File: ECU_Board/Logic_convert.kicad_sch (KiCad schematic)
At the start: 25 parts, among them U10 LM324A, U11 LM324A, U12 CD4504B, U13 CD4504B, U14 CD4504B

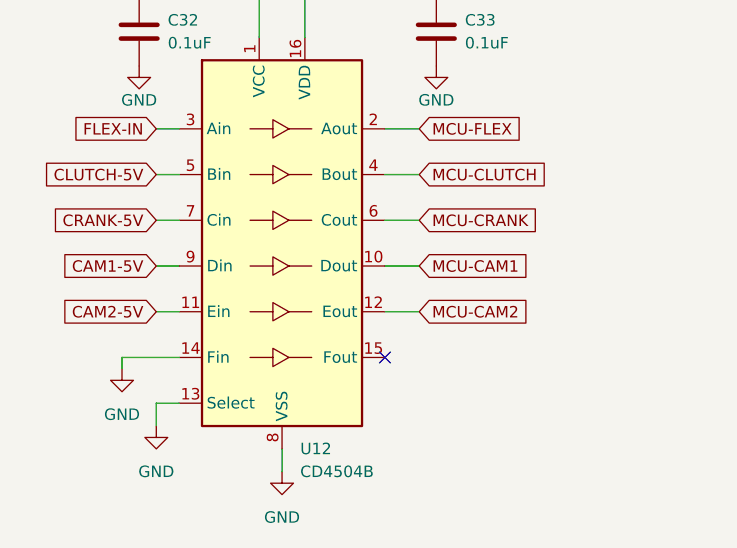
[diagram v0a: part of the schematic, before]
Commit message: Removed clutch input
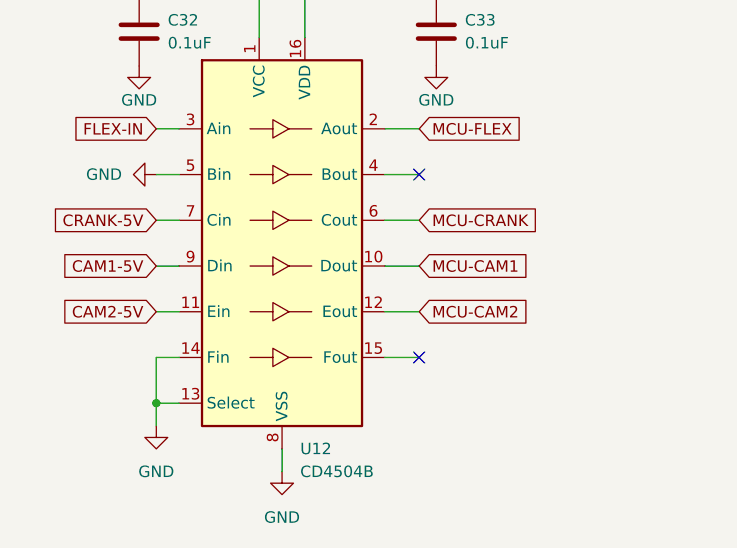
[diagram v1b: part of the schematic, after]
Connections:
- net CLUTCH-5V is gone; now on net GND: U12.5 (Bin)
- net MCU-CLUTCH: no longer names the net of U12.4 (Bout)
- no-connect marks 11 -> 12
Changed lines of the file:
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@@
   (title_block
     (title "Speeduino board for Teensy 4.1")
-    (date "2023-01-02")
-    (rev "5")
+    (date "2023-01-07")
+    (rev "6")
     (company "Fontys Eindhoven EXPO group 13 || Speeduino")
     (comment 1 "Adapted from Speeduino V0.4.4c board")
@@
   (junction (at 83.185 100.33) (diameter 0) (color 0 0 0 0)
   )
+  (junction (at 52.07 146.05) (diameter 0) (color 0 0 0 0)
+  )
   (junction (at 63.5 50.8) (diameter 0) (color 0 0 0 0)
   )
@@
   )
   (no_connect (at 173.99 85.09))
-  (no_connect (at 77.47 140.97))
   (no_connect (at 218.44 135.89))
   (no_connect (at 171.45 69.85))
@@
   (no_connect (at 163.83 140.97))
   (no_connect (at 224.79 69.85))
+  (no_connect (at 81.28 140.97))
   (no_connect (at 219.71 69.85))
   (no_connect (at 176.53 69.85))
   (no_connect (at 222.25 85.09))
+  (no_connect (at 81.28 120.65))
   (no_connect (at 218.44 130.81))
   (wire (pts (xy 134.62 135.89) (xy 137.16 135.89))
@@
     (stroke (width 0) (type default) (color 0 0 0 0))
   )
+  (wire (pts (xy 54.61 140.97) (xy 52.07 140.97))
+    (stroke (width 0) (type default) (color 0 0 0 0))
+  )
   (wire (pts (xy 106.68 49.53) (xy 109.22 49.53))
     (stroke (width 0) (type default) (color 0 0 0 0))
@@
     (stroke (width 0) (type default) (color 0 0 0 0))
   )
+  (wire (pts (xy 52.07 140.97) (xy 52.07 146.05))
+    (stroke (width 0) (type default) (color 0 0 0 0))
+  )
   (wire (pts (xy 106.68 88.9) (xy 109.22 88.9))
     (stroke (width 0) (type default) (color 0 0 0 0))
@@
     (stroke (width 0) (type default) (color 0 0 0 0))
   )
-  (wire (pts (xy 54.61 140.97) (xy 48.26 140.97))
-    (stroke (width 0) (type default) (color 0 0 0 0))
-  )
   (wire (pts (xy 77.47 115.57) (xy 81.28 115.57))
     (stroke (width 0) (type default) (color 0 0 0 0))
   )
+  (wire (pts (xy 77.47 140.97) (xy 81.28 140.97))
+    (stroke (width 0) (type default) (color 0 0 0 0))
+  )
   (wire (pts (xy 80.01 66.04) (xy 82.55 66.04))
     (stroke (width 0) (type default) (color 0 0 0 0))
@@
   )
   (wire (pts (xy 106.68 66.04) (xy 109.22 66.04))
-    (stroke (width 0) (type default) (color 0 0 0 0))
-  )
-  (wire (pts (xy 48.26 140.97) (xy 48.26 142.24))
     (stroke (width 0) (type default) (color 0 0 0 0))
   )
@@
     )
   )
-  (global_label "CLUTCH-5V" (shape input) (at 52.07 120.65 180) (fields_autoplaced)
-    (effects (font (size 1.27 1.27)) (justify right))
-    (property "Intersheet References" "${INTERSHEET_REFS}" (id 0) (at 38.5898 120.5706 0)
-      (effects (font (size 1.27 1.27)) (justify right) hide)
-    )
-  )
   (global_label "MCU-IDLE" (shape input) (at 134.62 120.65 180) (fields_autoplaced)
     (effects (font (size 1.27 1.27)) (justify right))
@@
     (property "Intersheet References" "${INTERSHEET_REFS}" (id 0) (at 180.8902 125.6506 0)
       (effects (font (size 1.27 1.27)) (justify right) hide)
-    )
-  )
-  (global_label "MCU-CLUTCH" (shape input) (at 81.28 120.65 0) (fields_autoplaced)
-    (effects (font (size 1.27 1.27)) (justify left))
-    (property "Intersheet References" "${INTERSHEET_REFS}" (id 0) (at 96.5141 120.5706 0)
-      (effects (font (size 1.27 1.27)) (justify left) hide)
     )
   )
@@
     (pin "1")
   )
+  (symbol (lib_id "power:GND") (at 52.07 120.65 270) (unit 1)
+    (in_bom yes) (on_board yes) (fields_autoplaced)
+    (property "Reference" "#PWR0142" (id 0) (at 45.72 120.65 0)
+      (effects (font (size 1.27 1.27)) hide)
+    )
+    (property "Value" "GND" (id 1) (at 48.26 120.6499 90)
+      (effects (font (size 1.27 1.27)) (justify right))
+    )
+    (property "Footprint" "" (id 2) (at 52.07 120.65 0)
+      (effects (font (size 1.27 1.27)) hide)
+    )
+    (property "Datasheet" "" (id 3) (at 52.07 120.65 0)
+      (effects (font (size 1.27 1.27)) hide)
+    )
+    (pin "1")
+  )
   (symbol (lib_id "power:GND") (at 134.62 148.59 0) (unit 1)
     (in_bom yes) (on_board yes) (fields_autoplaced)
@@
     (pin "2")
   )
-  (symbol (lib_id "power:GND") (at 48.26 142.24 0) (unit 1)
-    (in_bom yes) (on_board yes) (fields_autoplaced)
-    (property "Reference" "#PWR0227" (id 0) (at 48.26 148.59 0)
-      (effects (font (size 1.27 1.27)) hide)
-    )
-    (property "Value" "GND" (id 1) (at 48.26 147.32 0))
-    (property "Footprint" "" (id 2) (at 48.26 142.24 0)
-      (effects (font (size 1.27 1.27)) hide)
-    )
-    (property "Datasheet" "" (id 3) (at 48.26 142.24 0)
-      (effects (font (size 1.27 1.27)) hide)
-    )
-    (pin "1")
-  )
   (symbol (lib_id "power:GND") (at 224.155 108.585 0) (unit 1)

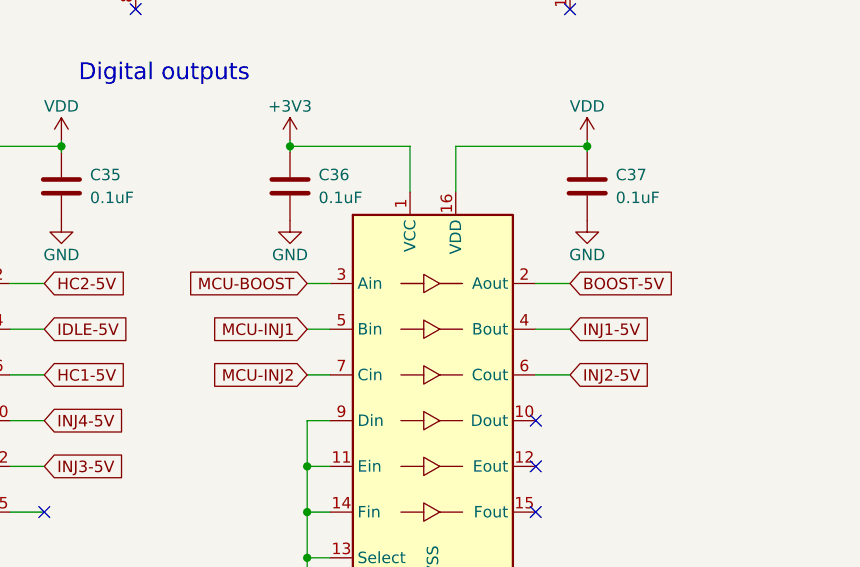
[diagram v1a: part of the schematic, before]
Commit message: Changed Boost output to ACIS
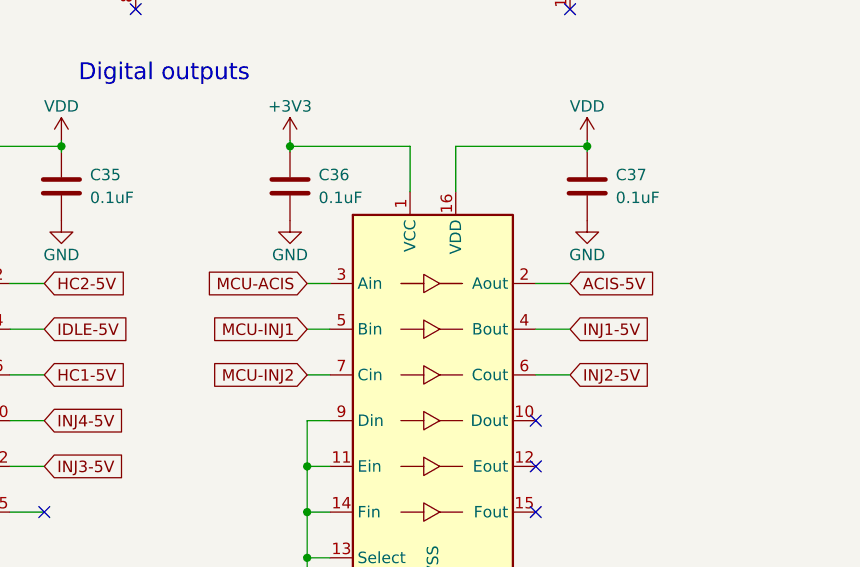
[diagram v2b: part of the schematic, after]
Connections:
- net BOOST-5V renamed ACIS-5V
- net MCU-BOOST renamed MCU-ACIS
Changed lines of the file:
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@@
     )
   )
-  (global_label "BOOST-5V" (shape input) (at 222.25 115.57 0) (fields_autoplaced)
+  (global_label "ACIS-5V" (shape input) (at 222.25 115.57 0) (fields_autoplaced)
     (effects (font (size 1.27 1.27)) (justify left))
-    (property "Intersheet References" "${INTERSHEET_REFS}" (id 0) (at 234.6417 115.4906 0)
+    (property "Intersheet References" "${INTERSHEET_REFS}" (id 0) (at 232.7064 115.4906 0)
       (effects (font (size 1.27 1.27)) (justify left) hide)
     )
   )
-  (global_label "MCU-BOOST" (shape input) (at 193.04 115.57 180) (fields_autoplaced)
+  (global_label "MCU-ACIS" (shape input) (at 193.04 115.57 180) (fields_autoplaced)
     (effects (font (size 1.27 1.27)) (justify right))
-    (property "Intersheet References" "${INTERSHEET_REFS}" (id 0) (at 178.8945 115.4906 0)
+    (property "Intersheet References" "${INTERSHEET_REFS}" (id 0) (at 180.8298 115.4906 0)
       (effects (font (size 1.27 1.27)) (justify right) hide)
     )
